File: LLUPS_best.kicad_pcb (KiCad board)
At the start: 2 copper layers, 140 x 90 mm, 39 parts, among them J1 USB_C, J2 Output, J3 Debug, Q1 FS8205A, U1 USBLC6-2SC6, U2 BQ24072, U3 HY2113-KB5B, U4 MT3608, U5 AP2112K-3.3, U6 LN61CN3302MR-G

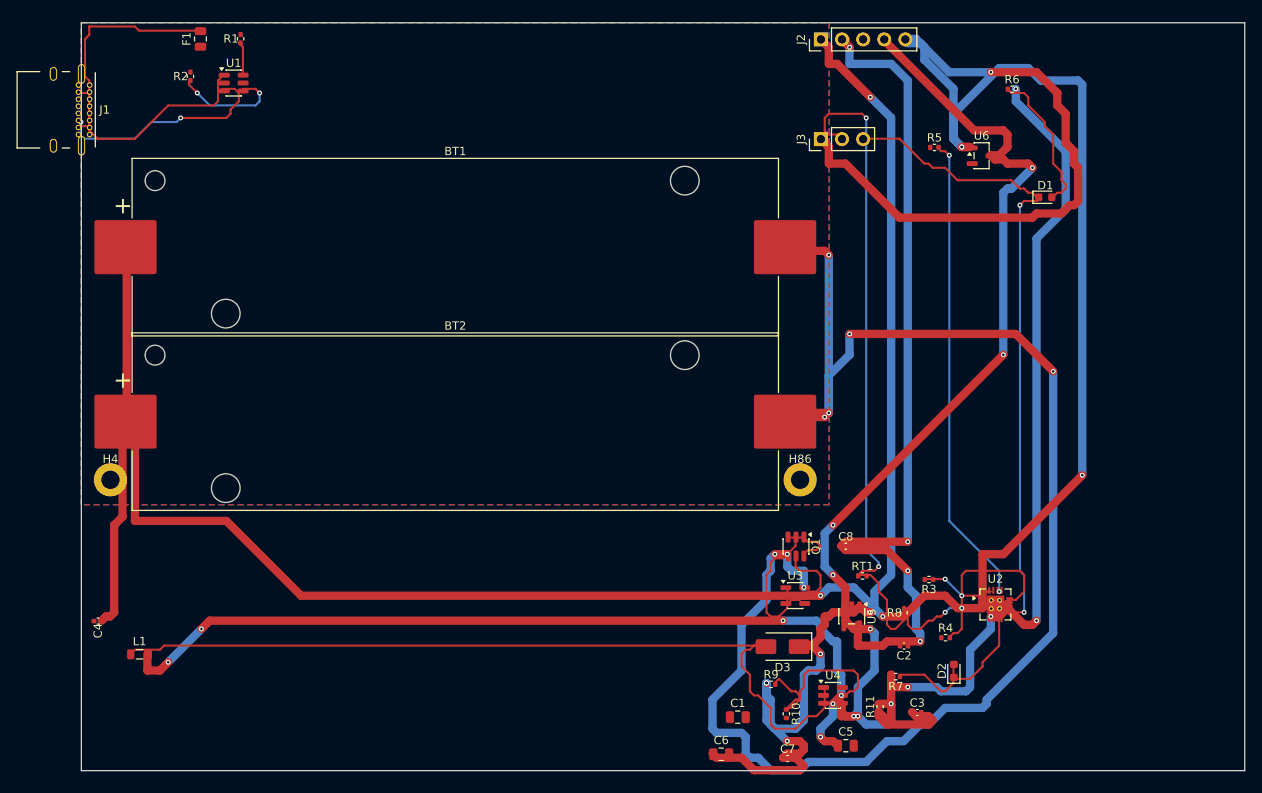
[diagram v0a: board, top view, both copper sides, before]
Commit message: 35-round experiment: best score 25.33, improved routing params
Router and conflict resolution tuning from autonomous optimization loop.
Best config: clearance=0.2051mm, cooling_factor=0.9735, existing_trace_cost=200.0

Co-Authored-By: Claude Opus 4.6 <noreply@anthropic.com>
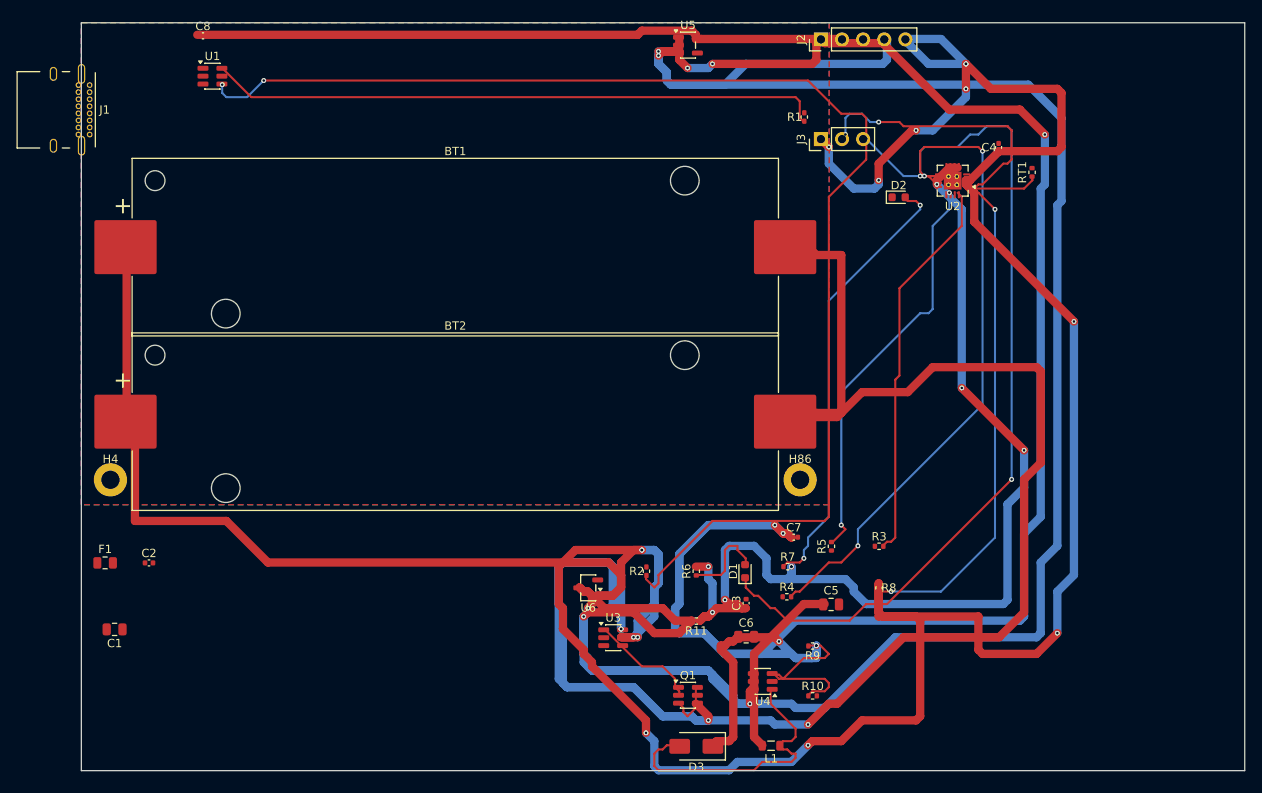
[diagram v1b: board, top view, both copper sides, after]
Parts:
- moved C4 122.5 mm to (110.4, 15.0), turned to 90 degrees
- moved C8 98.8 mm to (14.6, 1.57)
- moved C2 91.4 mm to (8.14, 65.0), turned to 0 degrees
- moved R2 81.0 mm to (68.0, 66.0)
- moved L1 76.8 mm to (83.0, 87.0), turned to 180 degrees
- moved C1 75.7 mm to (4.00, 73.0), turned to 180 degrees
- moved U5 71.5 mm to (73.0, 2.69), turned to 0 degrees
- moved U6 70.3 mm to (61.0, 68.0), turned to 180 degrees
- moved R6 69.3 mm to (74.0, 66.0), turned to 90 degrees
- moved R1 68.5 mm to (87.0, 11.3)
- moved F1 64.1 mm to (2.86, 65.0), turned to 0 degrees
- moved D1 57.7 mm to (79.9, 66.0), turned to 90 degrees
- moved D2 57.4 mm to (98.4, 21.0), turned to 0 degrees
- moved RT1 52.7 mm to (114.4, 18.0), turned to 90 degrees
- moved U2 51.3 mm to (104.9, 19.0), turned to 180 degrees
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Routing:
- net /EN: track 125.0 -> 289.1 mm, vias 8 -> 6
- net Net-(R2-Pad1): track 13.4 -> 158.3 mm
- net /5V: track 136.6 -> 256.6 mm, vias 6 -> 8
- net /VSYS_BOOST: track 104.0 -> 22.4 mm, vias 6 -> 0
- net Net-(R1-Pad1): track 4.21 -> 73.9 mm
- net Net-(D3-A): track 100.8 -> 34.8 mm
- net Net-(U2-ILIM): track 20.7 -> 77.7 mm, vias 0 -> 2
- net /VBAT: track 351.6 -> 406.9 mm, vias 8 -> 16
- net /CELL_NEG: track 187.8 -> 240.8 mm, vias 8 -> 4
- net Net-(D2-A): track 9.74 -> 53.6 mm, vias 0 -> 2
- net Net-(U2-ISET): track 9.04 -> 46.9 mm, vias 2 -> 0
- net /CHG_N: track 78.5 -> 111.7 mm, vias 2 -> 4
- net Net-(F1-Pad2): track 28.1 -> 0.00 mm
- net Net-(J1-CC2): track 26.4 -> 0.00 mm, vias 2 -> 0
- net /3V3: track 103.8 -> 78.4 mm, vias 4 -> 0
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
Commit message: Update baseline: 5mil traces achieve 29.0 score
Next experiment will iterate from this best layout.

Co-Authored-By: Claude Opus 4.6 <noreply@anthropic.com>
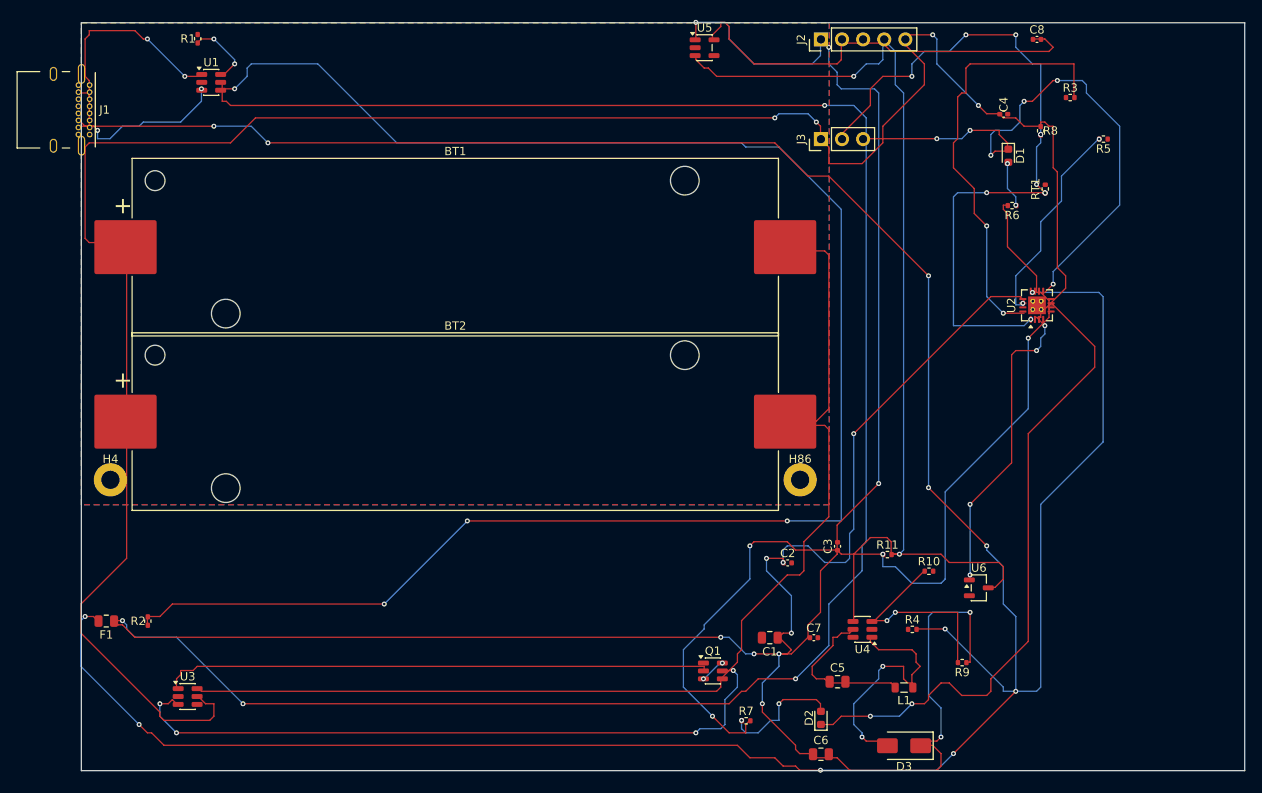
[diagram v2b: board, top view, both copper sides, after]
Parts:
- moved C8 100.4 mm to (115.0, 2.00)
- moved C1 78.9 mm to (82.8, 74.0)
- moved C2 76.9 mm to (85.0, 65.0)
- moved R1 73.6 mm to (14.0, 1.92)
- moved D2 63.3 mm to (89.0, 83.6), turned to 90 degrees
- moved R2 60.3 mm to (8.00, 72.0)
- moved D1 59.2 mm to (111.6, 16.0), turned to -90 degrees
- moved R5 58.9 mm to (123.0, 14.0), turned to 180 degrees
- moved R3 58.7 mm to (119.0, 9.00)
- moved R8 58.3 mm to (115.4, 13.0)
- moved R6 58.1 mm to (112.0, 22.0), turned to 180 degrees
- moved U3 51.7 mm to (12.8, 81.1)
- moved U6 47.0 mm to (108.0, 68.0), turned to 0 degrees
- moved D3 25.0 mm to (99.0, 87.0)
- moved R11 24.4 mm to (97.0, 64.0), turned to 0 degrees
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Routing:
- net /VBUS: track 0.00 -> 393.0 mm, vias 0 -> 10
- net Net-(F1-Pad2): track 0.00 -> 298.3 mm, vias 0 -> 10
- net /EN: track 289.1 -> 124.8 mm, vias 6 -> 4
- net /VBAT: track 406.9 -> 296.8 mm, vias 16 -> 8
- net /CELL_NEG: track 240.8 -> 137.1 mm, vias 4 -> 0
- net /5V: track 256.6 -> 174.3 mm
- net Net-(Q1B-G): track 0.00 -> 82.0 mm, vias 0 -> 4
- net Net-(D2-K): track 0.00 -> 77.9 mm, vias 0 -> 2
- net Net-(R1-Pad1): track 73.9 -> 8.36 mm, vias 0 -> 2
- net Net-(Q1A-G): track 13.2 -> 65.9 mm
- net Net-(R2-Pad1): track 158.3 -> 210.3 mm, vias 2 -> 4
- net /CHG_N: track 111.7 -> 70.5 mm, vias 4 -> 6
- net Net-(D2-A): track 53.6 -> 14.7 mm
- net /3V3: track 78.4 -> 51.8 mm
- net Net-(J1-CC1): track 0.00 -> 24.2 mm, vias 0 -> 2
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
